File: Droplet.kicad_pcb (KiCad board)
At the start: 2 copper layers, 40.8 x 37.8 mm, 15 parts, among them J1 Conn_01x05, J2 Conn_01x05, J3 Prog, U1 ATtiny202-SS, U2 IRM-H6xxT

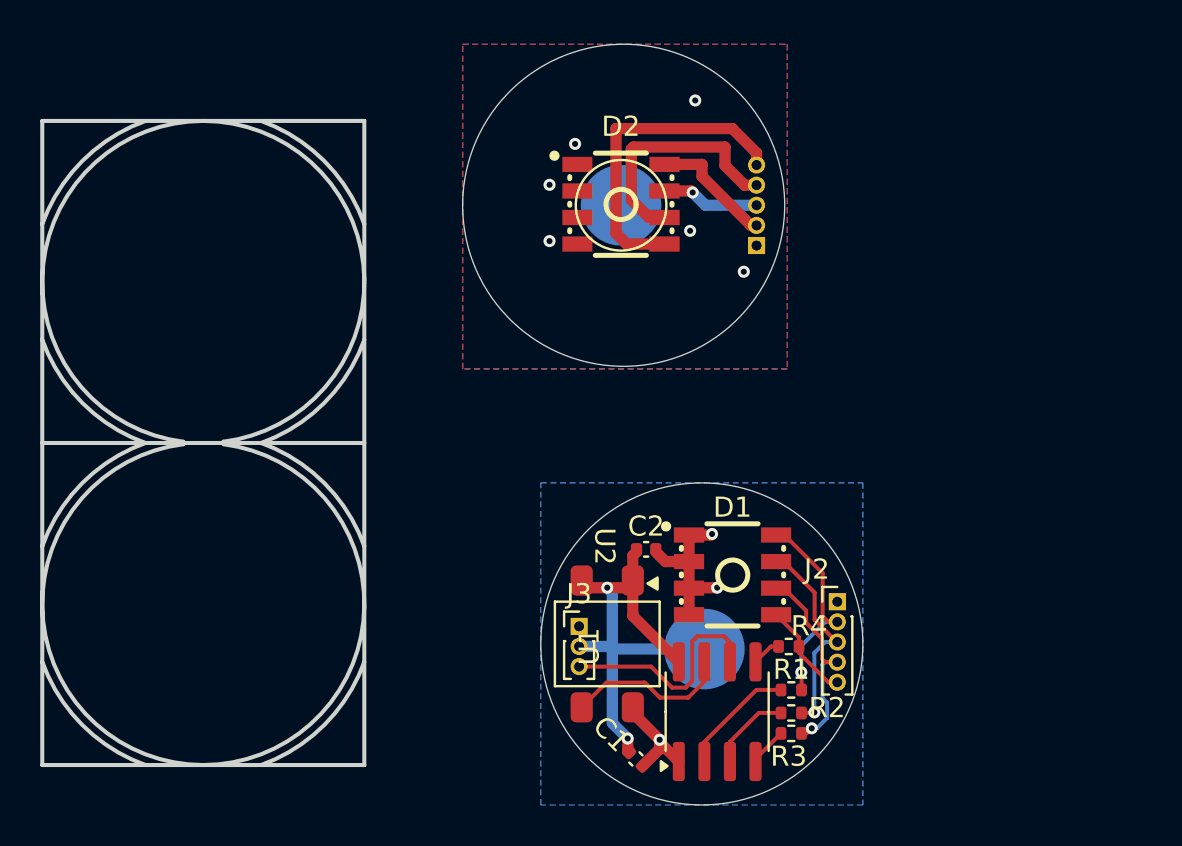
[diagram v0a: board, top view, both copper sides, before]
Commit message: do layout, including mouse bites
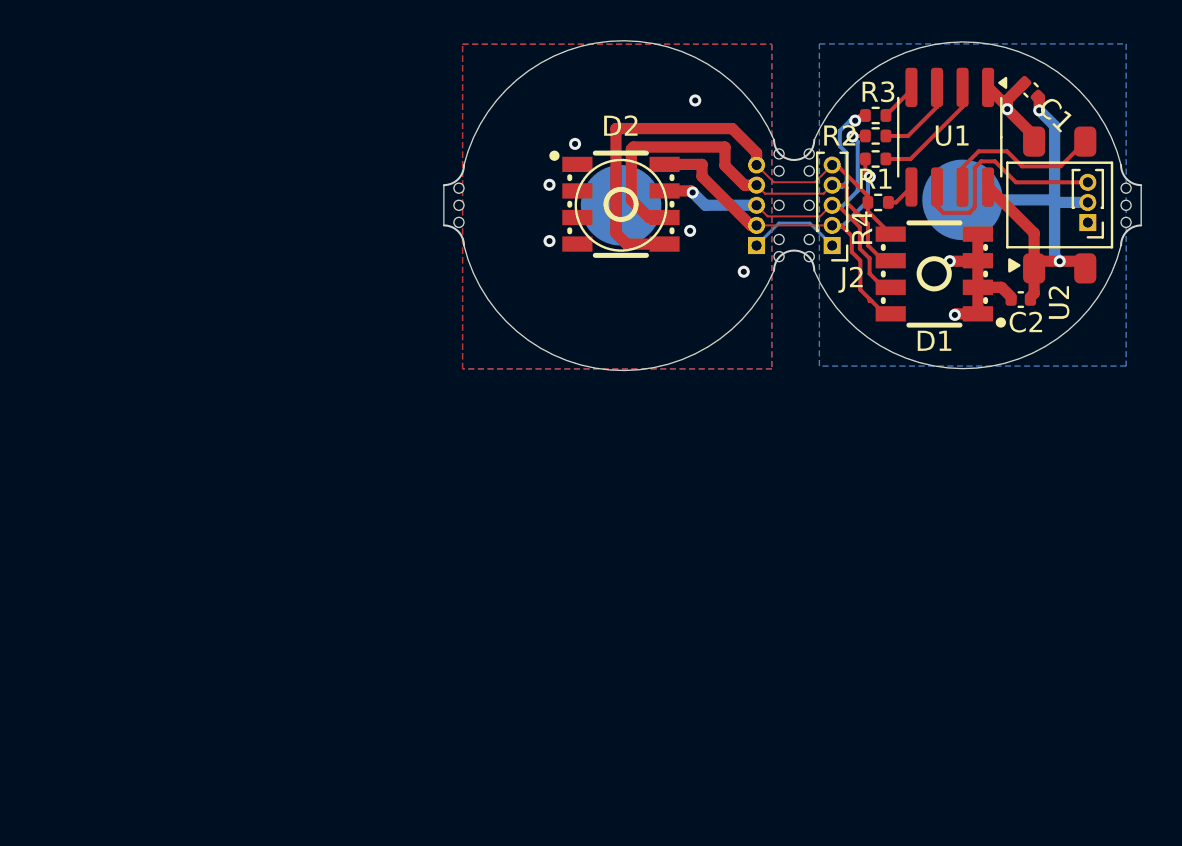
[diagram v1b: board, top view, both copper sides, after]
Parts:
- added REF**: MouseBite-Part_2.0x2.0mm_outset_D0.5mm_P0.85mm_3h, Panelization:MouseBite-Part_2.0x2.0mm_outset_D0.5mm_P0.85mm_3h, F.Cu at (126.2, 35.3)
- added REF**: MouseBite-Slot_2.0x4.5mm_outset_D0.5mm_P0.85mm_5h_Trace, Panelization:MouseBite-Slot_2.0x4.5mm_outset_D0.5mm_P0.85mm_5h_Trace, F.Cu at (111.0, 35.3)
- added REF**: MouseBite-Part_2.0x2.0mm_outset_D0.5mm_P0.85mm_3h, Panelization:MouseBite-Part_2.0x2.0mm_outset_D0.5mm_P0.85mm_3h, F.Cu at (93.6, 35.3)
- moved C1 38.6 mm to (121.8, 29.6), turned to -45 degrees
- moved J3 32.3 mm to (124.6, 36.2), turned to 180 degrees
- moved U2 31.3 mm to (123.2, 35.3), turned to 90 degrees
- moved R3 31.0 mm to (114.0, 30.8), turned to 0 degrees
- moved U1 30.8 mm to (117.7, 31.9), turned to -90 degrees
- moved R2 29.0 mm to (114.0, 31.9), turned to 0 degrees
- moved R1 26.7 mm to (114.0, 33.0), turned to 180 degrees
- moved TP2 25.7 mm to (118.4, 35.0), turned to 0 degrees
- moved R4 22.5 mm to (114.2, 35.2), turned to 0 degrees
- moved C2 22.4 mm to (121.3, 40.0), turned to 0 degrees
- moved D1 18.0 mm to (117.0, 38.7), turned to 180 degrees
- moved J2 17.7 mm to (111.9, 37.3), turned to 180 degrees
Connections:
- D1 pad 5: Net-(J2-Pin_2) -> Net-(J1-Pin_2)
- D1 pad 6: Net-(J2-Pin_3) -> Net-(J1-Pin_3)
- D1 pad 7: Net-(J2-Pin_4) -> Net-(J1-Pin_4)
- D1 pad 8: Net-(J2-Pin_5) -> Net-(J1-Pin_5)
- D2 pad 1: Net-(J1-Pin_1) -> VBATT
- D2 pad 2: Net-(J1-Pin_1) -> VBATT
- D2 pad 3: Net-(J1-Pin_1) -> VBATT
- D2 pad 4: Net-(J1-Pin_1) -> VBATT
- J1 pad 1: Net-(J1-Pin_1) -> VBATT
- J2 pad 2: Net-(J2-Pin_2) -> Net-(J1-Pin_2)
- J2 pad 3: Net-(J2-Pin_3) -> Net-(J1-Pin_3)
- J2 pad 4: Net-(J2-Pin_4) -> Net-(J1-Pin_4)
- J2 pad 5: Net-(J2-Pin_5) -> Net-(J1-Pin_5)
- R1 pad 2: Net-(J2-Pin_2) -> Net-(J1-Pin_2)
- R2 pad 1: Net-(J2-Pin_3) -> Net-(J1-Pin_3)
- R3 pad 1: Net-(J2-Pin_4) -> Net-(J1-Pin_4)
- R4 pad 1: Net-(J2-Pin_5) -> Net-(J1-Pin_5)
- TP1 pad 1: Net-(J1-Pin_1) -> VBATT
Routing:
- net Net-(J1-Pin_3): track 4.87 -> 20.6 mm, vias 1 -> 2
- net Net-(J1-Pin_4): track 12.1 -> 27.2 mm, vias 0 -> 1
- net Net-(J1-Pin_2): track 6.18 -> 21.3 mm, vias 0 -> 1
- net Net-(J2-Pin_4): track 10.6 -> 0.00 mm, vias 1 -> 0
- net Net-(J2-Pin_2): track 10.6 -> 0.00 mm, vias 1 -> 0
- net Net-(J2-Pin_3): track 10.5 -> 0.00 mm, vias 1 -> 0
- net Net-(J1-Pin_5): track 15.7 -> 25.1 mm
- net Net-(J2-Pin_5): track 4.94 -> 0.00 mm
- net VBATT: track 13.4 -> 18.1 mm, vias 3 -> 9
- net Net-(J1-Pin_1): vias 6 -> 0
- added copper zone on F.Cu, net VBATT
- removed copper zone on B.Cu, net Net-(J1-Pin_1)
- removed copper zone on F.Cu, net Net-(J1-Pin_1)
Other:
- board size 40.8 x 37.8 mm -> 34.6 x 16.4 mm

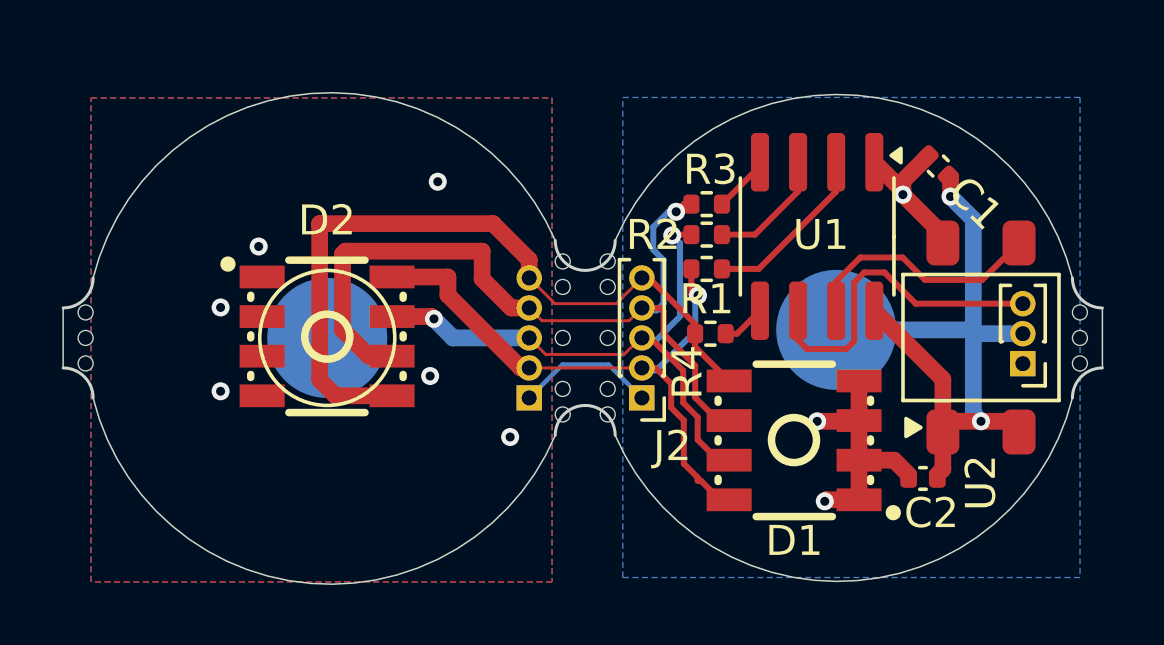
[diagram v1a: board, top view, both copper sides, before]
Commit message: update to use warm white RGB LED. Single unit layout
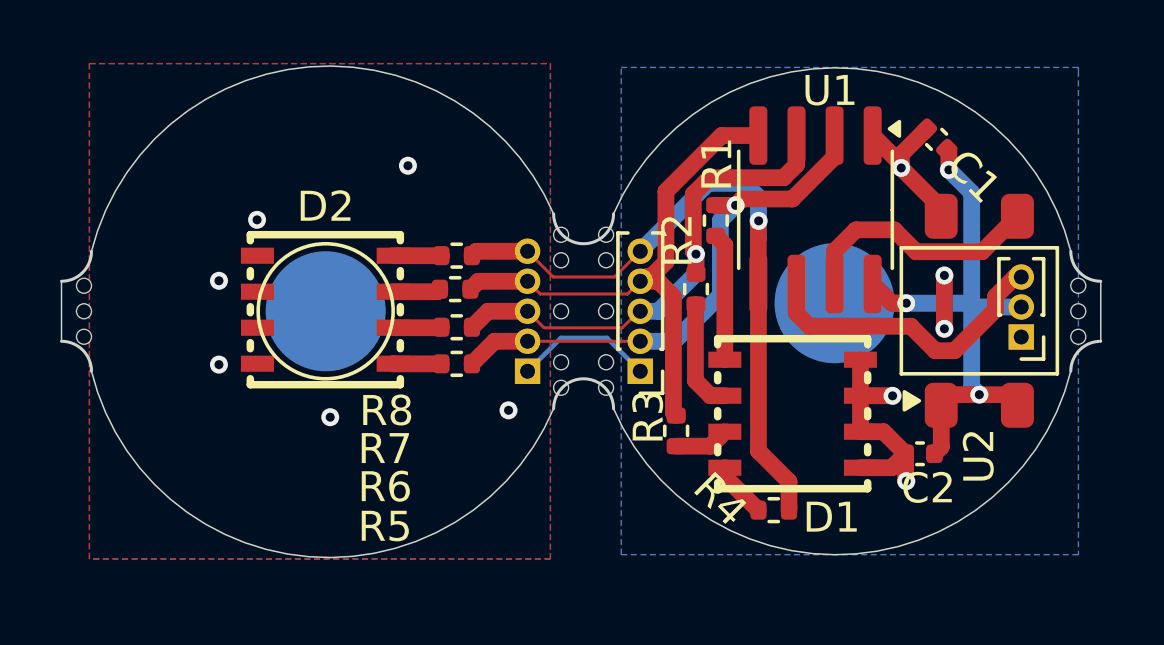
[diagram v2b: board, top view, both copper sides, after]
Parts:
- added R5: 22, Resistor_SMD:R_0402_1005Metric, F.Cu at (105.7, 36.2)
- added R6: 22, Resistor_SMD:R_0402_1005Metric, F.Cu at (105.7, 35.0)
- added R7: 22, Resistor_SMD:R_0402_1005Metric, F.Cu at (105.7, 33.7)
- added R8: 47, Resistor_SMD:R_0402_1005Metric, F.Cu at (105.7, 32.6)
- D1, D2: value XL-5050RGBW -> HL-5050RGBW-S1-A27; footprint EasyEDA-Imports:LED-SMD_8P-L5.0-W5.0-P1.32-TL -> easyeda2kicad:LED-SMD_8P-L5.0-W5.0-P1.20_HL-5050RGBW-S1-A27
- R1: value 47 -> 22
- R4: value 22 -> 47
- U2: value IRM-H6xxT -> IRM-H638T/TR2
- moved R3 7.63 mm to (113.0, 38.4), turned to -90 degrees
- moved R4 6.25 mm to (116.3, 41.0), turned to 180 degrees
- moved R2 1.85 mm to (113.7, 33.7), turned to -90 degrees
- moved R1 1.64 mm to (114.4, 31.4), turned to 90 degrees
- moved J2 0.89 mm to (111.8, 36.4)
- moved TP2 0.89 mm to (118.3, 34.1)
- moved C1 0.89 mm to (121.7, 28.7)
- moved U1 0.89 mm to (117.7, 31.0)
- moved D1 0.89 mm to (116.9, 37.8), turned to 0 degrees
- moved D2 0.89 mm to (101.3, 34.4), turned to 180 degrees
- moved J1 0.89 mm to (108.1, 36.4)
- moved J3 0.89 mm to (124.5, 35.3)
- moved REF** 0.89 mm to (126.2, 34.4)
- moved REF** 0.89 mm to (110.9, 34.4)
- moved REF** 0.89 mm to (93.5, 34.4)
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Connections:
- D1 pad 2: VBATT -> Net-(D1-Pad2)
- D1 pad 4: VBATT -> Net-(D1-Pad4)
- D1 pad 5: Net-(J1-Pin_2) -> VBATT
- D1 pad 6: Net-(J1-Pin_3) -> Net-(D1-Pad6)
- D1 pad 7: Net-(J1-Pin_4) -> VBATT
- D1 pad 8: Net-(J1-Pin_5) -> Net-(D1-Pad8)
- D2 pad 2: VBATT -> Net-(D2-Pad2)
- D2 pad 4: VBATT -> Net-(D2-Pad4)
- D2 pad 5: Net-(J1-Pin_2) -> VBATT
- D2 pad 6: Net-(J1-Pin_3) -> Net-(D2-Pad6)
- D2 pad 7: Net-(J1-Pin_4) -> VBATT
- D2 pad 8: Net-(J1-Pin_5) -> Net-(D2-Pad8)
- R1 pad 1: Net-(U1-PA6) -> Net-(D1-Pad2)
- R2 pad 2: Net-(U1-PA7) -> Net-(D1-Pad4)
- R3 pad 2: Net-(U1-PA1) -> Net-(D1-Pad6)
- R4 pad 2: Net-(U1-PA2) -> Net-(D1-Pad8)
- U1 pad 2: Net-(U1-PA6) -> Net-(J1-Pin_2)
- U1 pad 3: Net-(U1-PA7) -> Net-(J1-Pin_3)
- U1 pad 4: Net-(U1-PA1) -> Net-(J1-Pin_4)
- U1 pad 5: Net-(U1-PA2) -> Net-(J1-Pin_5)
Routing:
- net Net-(J1-Pin_4): track 27.2 -> 19.3 mm, vias 1 -> 0
- net Net-(U1-PA6): track 5.85 -> 0.00 mm
- net Net-(D1-Pad2): track 0.00 -> 4.32 mm
- net Net-(U1-PA7): track 4.11 -> 0.00 mm
- net Net-(D1-Pad4): track 0.00 -> 3.74 mm
- net GND: track 24.0 -> 20.6 mm, vias 2 -> 3
- net Net-(J1-Pin_3): track 20.6 -> 17.3 mm, vias 2 -> 1
- net Net-(D1-Pad6): track 0.00 -> 2.96 mm
- net Net-(J1-Pin_5): track 25.1 -> 22.3 mm, vias 0 -> 1
- net Net-(J1-Pin_2): track 21.3 -> 18.5 mm
- net Net-(U1-PA1): track 1.92 -> 0.00 mm
- net Net-(D1-Pad8): track 0.00 -> 1.88 mm
- net Net-(D2-Pad4): track 0.00 -> 1.62 mm
- net Net-(D2-Pad2): track 0.00 -> 1.61 mm
- net Net-(D2-Pad8): track 0.00 -> 1.61 mm
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
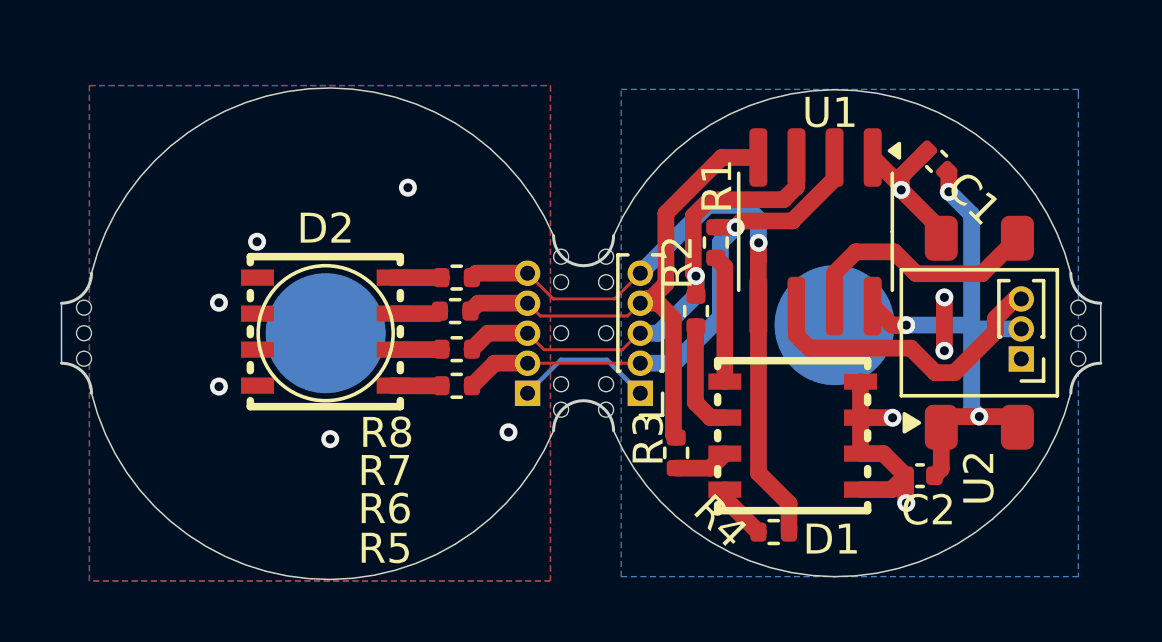
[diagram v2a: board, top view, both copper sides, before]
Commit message: rework with castellated connectors
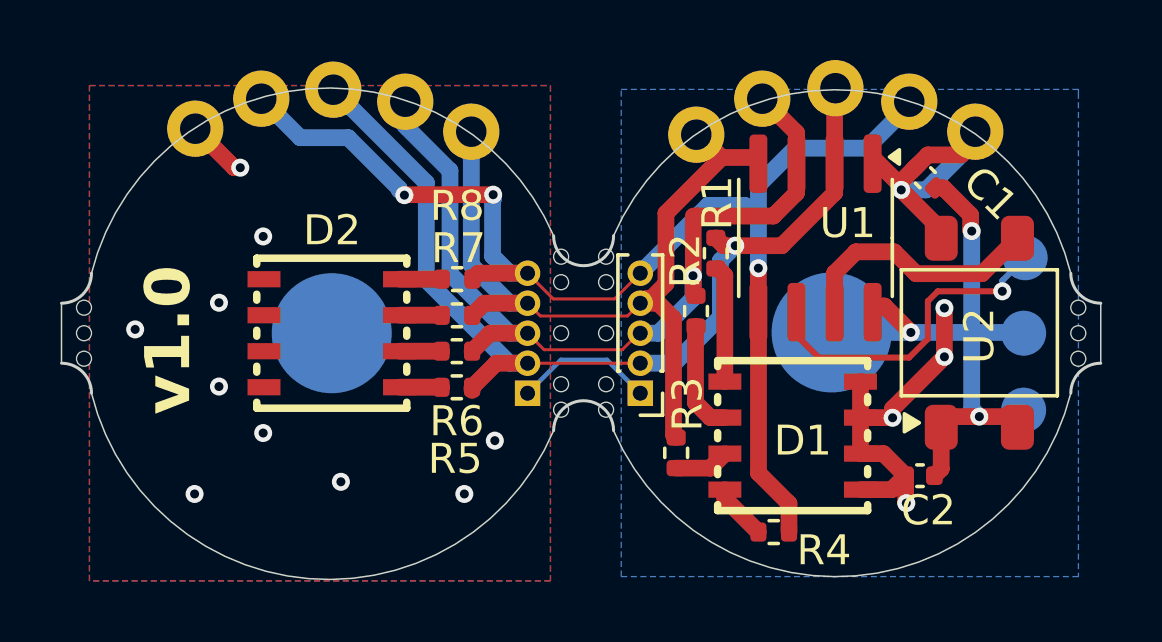
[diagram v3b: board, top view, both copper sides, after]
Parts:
- added J10: Conn_01x01, Custom:1x01_P2.54mm castellated, F.Cu at (104.0, 26.7)
- added J11: Conn_01x01, Custom:1x01_P2.54mm castellated, F.Cu at (101.6, 26.3)
- added J12: Conn_01x01, Custom:1x01_P2.54mm castellated, F.Cu at (97.0, 27.6)
- added J4: Conn_01x01, Custom:1x01_P2.54mm castellated, F.Cu at (115.9, 26.6)
- added J5: Conn_01x01, Custom:1x01_P2.54mm castellated, F.Cu at (113.7, 27.8)
- added J6: Conn_01x01, Custom:1x01_P2.54mm castellated, F.Cu at (120.8, 26.7)
- added J7: Conn_01x01, Custom:1x01_P2.54mm castellated, F.Cu at (123.0, 27.7)
- added J8: Conn_01x01, Custom:1x01_P2.54mm castellated, F.Cu at (99.2, 26.6)
- added J9: Conn_01x01, Custom:1x01_P2.54mm castellated, F.Cu at (106.2, 27.7)
- added TP3: PA0, TestPoint:TestPoint_Pad_D1.5mm, B.Cu at (124.7, 31.9)
- added TP4: -, TestPoint:TestPoint_Pad_D1.5mm, B.Cu at (124.6, 34.4)
- added TP5: VBATT, TestPoint:TestPoint_Pad_D1.5mm, B.Cu at (124.6, 37.0)
- J3: value Prog -> Conn_01x01; footprint Connector_PinHeader_1.00mm:PinHeader_1x03_P1.00mm_Vertical -> Custom:1x01_P2.54mm castellated
- R1, R2, R3, R5, R6, R7: value 22 -> 27
- R4, R8: value 47 -> 75
- TP1: moved to B.Cu
- moved J3 10.9 mm to (118.3, 26.2), turned to 90 degrees
- moved C1 0.66 mm to (121.3, 29.2)
- moved R1 0.36 mm to (114.4, 31.8)
- moved TP2 0.26 mm to (118.2, 34.4)
- moved D2 0.22 mm to (101.5, 34.4)
- moved U1 0.21 mm to (117.7, 31.2)
- moved TP1 0.20 mm to (101.5, 34.4), turned to 180 degrees
- moved R7 0.15 mm to (105.7, 33.8)
- moved R6 0.07 mm to (105.7, 35.0)
- moved R8 0.05 mm to (105.7, 32.6)
- moved R5 0.05 mm to (105.7, 36.2)
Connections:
- net Net-(J1-Pin_3) renamed /PA7
- net Net-(J1-Pin_4) renamed /PA1
- net Net-(J1-Pin_5) renamed /PA2
- net Net-(U1-PA3) renamed /PA3
- J1 pad 2: Net-(J1-Pin_2) -> /PA6
- J2 pad 2: Net-(J1-Pin_2) -> /PA6
- J3 pad 1: VBATT -> /PA6
- R1 pad 2: Net-(J1-Pin_2) -> /PA6
- R5 pad 1: Net-(J1-Pin_2) -> /PA6
- U1 pad 2: Net-(J1-Pin_2) -> /PA6
- U1 pad 6: Net-(J3-Pin_3) -> /PA0
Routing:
- net /PA6: track 0.00 -> 33.2 mm, vias 0 -> 1
- net /PA2: track 22.3 -> 42.2 mm, vias 1 -> 3
- net Net-(J1-Pin_2): track 18.5 -> 0.00 mm, vias 1 -> 0
- net /PA7: track 17.3 -> 30.6 mm
- net /PA0: track 0.00 -> 11.2 mm, vias 0 -> 1
- net Net-(J3-Pin_3): track 10.3 -> 0.00 mm
- net VBATT: track 19.4 -> 29.3 mm, vias 11 -> 15
- net /PA1: track 19.3 -> 27.5 mm
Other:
- board text added: "1"
- board text added: "2"
- board text added: "3"
- board text added: "4"
- board text added: "5"
- board text added: "Brian Alvarez"
- board text added: "v1.0"

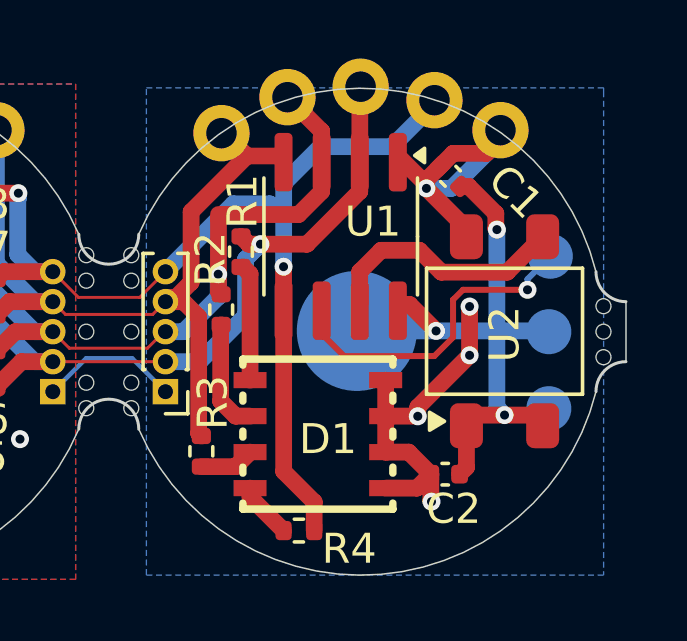
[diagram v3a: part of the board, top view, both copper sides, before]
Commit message: update schematic readability, rotate ir receiver
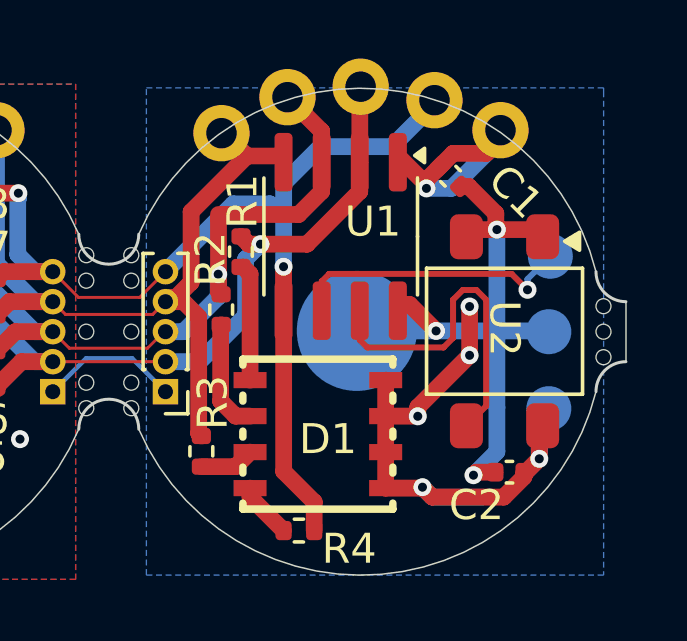
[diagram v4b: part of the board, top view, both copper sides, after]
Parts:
- moved C2 2.14 mm to (123.3, 39.1), turned to 180 degrees
- turned U2 to -90 degrees
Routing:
- net VBATT: track 29.3 -> 35.1 mm, vias 15 -> 16
- net /PA3: track 8.28 -> 11.4 mm
- net GND: track 20.7 -> 22.2 mm
- net /PA0: track 11.2 -> 10.6 mm
